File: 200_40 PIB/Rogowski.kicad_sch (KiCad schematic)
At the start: 8 parts, among them J6 53261-0271, U11 OP37

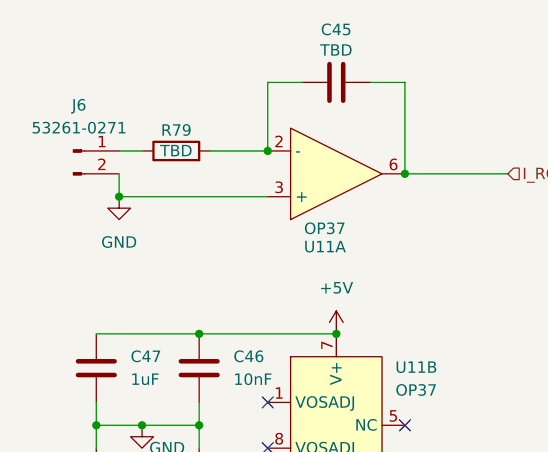
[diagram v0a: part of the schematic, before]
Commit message: assign PIB footprints, push ioc file to CubeMX 6.18.1
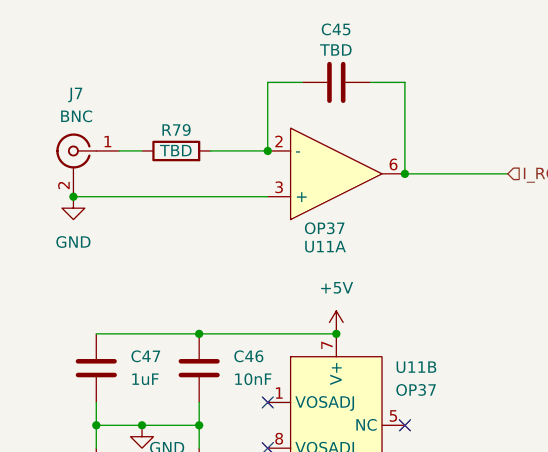
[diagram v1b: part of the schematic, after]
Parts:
- removed J6: 53261-0271, Connector_Molex:Molex_PicoBlade_53261-0271_1x02-1MP_P1.25mm_Horizontal, symbol Connector:Conn_01x02_Pin
- added J7: BNC, Connector_Coaxial:BNC_Amphenol_B6252HB-NPP3G-50_Horizontal, symbol Connector:Conn_Coaxial
- C45, C46, C47, C48, C49: footprint (none) -> Capacitor_SMD:C_0603_1608Metric
- R79: footprint (none) -> Resistor_SMD:R_0603_1608Metric
- U11: footprint Package_TO_SOT_SMD:SOT-353_SC-70-5 -> Package_SO:SOIC-8_3.9x4.9mm_P1.27mm
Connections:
- net GND: now also J7.2 (Ext)
- net at R79.1: now also J7.1 (In)
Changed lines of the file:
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@@
+	)
+	(junction
+		(at 54.61 71.12)
+		(diameter 0)
+		(color 0 0 0 0)
 	)
 	(junction
@@
 	)
 	(junction
-		(at 59.69 71.12)
-		(diameter 0)
-		(color 0 0 0 0)
-	)
-	(junction
 		(at 68.58 96.52)
 		(diameter 0)
@@
 	(wire
 		(pts
-			(xy 59.69 71.12) (xy 76.2 71.12)
+			(xy 54.61 71.12) (xy 76.2 71.12)
 		)
 		(stroke
@@
 		(pts
 			(xy 91.44 68.58) (xy 91.44 58.42)
-		)
-		(stroke
-			(width 0)
-			(type default)
-		)
-	)
-	(wire
-		(pts
-			(xy 59.69 71.12) (xy 59.69 68.58)
 		)
 		(stroke
@@
 			)
 		)
-		(property "Footprint" "Package_TO_SOT_SMD:SOT-353_SC-70-5"
+		(property "Footprint" "Package_SO:SOIC-8_3.9x4.9mm_P1.27mm"
 			(at 82.55 73.66 0)
 			(hide yes)
@@
 			)
 		)
-		(property "Footprint" ""
+		(property "Footprint" "Capacitor_SMD:C_0603_1608Metric"
 			(at 58.1152 93.98 0)
 			(hide yes)
@@
 				(path "/2bb2e4a1-de70-477a-a246-143db0a21e08/177725a5-a22e-4ba6-aa4d-305743e89374"
 					(reference "C47")
-					(unit 1)
-				)
-			)
-		)
-	)
-	(symbol
-		(lib_id "Connector:Conn_01x02_Pin")
-		(at 54.61 66.04 0)
-		(unit 1)
-		(body_style 1)
-		(exclude_from_sim no)
-		(in_bom yes)
-		(on_board yes)
-		(in_pos_files yes)
-		(dnp no)
-		(fields_autoplaced yes)
-		(property "Reference" "J6"
-			(at 55.245 60.96 0)
-			(show_name no)
-			(do_not_autoplace no)
-			(effects
-				(font
-					(size 1.27 1.27)
-				)
-			)
-		)
-		(property "Value" "53261-0271"
-			(at 55.245 63.5 0)
-			(show_name no)
-			(do_not_autoplace no)
-			(effects
-				(font
-					(size 1.27 1.27)
-				)
-			)
-		)
-		(property "Footprint" "Connector_Molex:Molex_PicoBlade_53261-0271_1x02-1MP_P1.25mm_Horizontal"
-			(at 54.61 66.04 0)
-			(hide yes)
-			(show_name no)
-			(do_not_autoplace no)
-			(effects
-				(font
-					(size 1.27 1.27)
-				)
-			)
-		)
-		(property "Datasheet" ""
-			(at 54.61 66.04 0)
-			(hide yes)
-			(show_name no)
-			(do_not_autoplace no)
-			(effects
-				(font
-					(size 1.27 1.27)
-				)
-			)
-		)
-		(property "Description" "Generic connector, single row, 01x02, script generated"
-			(at 54.61 66.04 0)
-			(hide yes)
-			(show_name no)
-			(do_not_autoplace no)
-			(effects
-				(font
-					(size 1.27 1.27)
-				)
-			)
-		)
-		(pin "2"
-		)
-		(pin "1"
-		)
-		(instances
-			(project "PIB"
-				(path "/2bb2e4a1-de70-477a-a246-143db0a21e08/177725a5-a22e-4ba6-aa4d-305743e89374"
-					(reference "J6")
 					(unit 1)
 				)
@@
 			)
 		)
-		(property "Footprint" ""
+		(property "Footprint" "Capacitor_SMD:C_0603_1608Metric"
 			(at 69.5452 106.68 0)
 			(hide yes)
@@
 				(path "/2bb2e4a1-de70-477a-a246-143db0a21e08/177725a5-a22e-4ba6-aa4d-305743e89374"
 					(reference "C49")
+					(unit 1)
+				)
+			)
+		)
+	)
+	(symbol
+		(lib_id "Connector:Conn_Coaxial")
+		(at 54.61 66.04 0)
+		(mirror y)
+		(unit 1)
+		(body_style 1)
+		(exclude_from_sim no)
+		(in_bom yes)
+		(on_board yes)
+		(in_pos_files yes)
+		(dnp no)
+		(fields_autoplaced yes)
+		(property "Reference" "J7"
+			(at 54.9274 59.69 0)
+			(show_name no)
+			(do_not_autoplace no)
+			(effects
+				(font
+					(size 1.27 1.27)
+				)
+			)
+		)
+		(property "Value" "BNC"
+			(at 54.9274 62.23 0)
+			(show_name no)
+			(do_not_autoplace no)
+			(effects
+				(font
+					(size 1.27 1.27)
+				)
+			)
+		)
+		(property "Footprint" "Connector_Coaxial:BNC_Amphenol_B6252HB-NPP3G-50_Horizontal"
+			(at 54.61 66.04 0)
+			(hide yes)
+			(show_name no)
+			(do_not_autoplace no)
+			(effects
+				(font
+					(size 1.27 1.27)
+				)
+			)
+		)
+		(property "Datasheet" ""
+			(at 54.61 66.04 0)
+			(hide yes)
+			(show_name no)
+			(do_not_autoplace no)
+			(effects
+				(font
+					(size 1.27 1.27)
+				)
+			)
+		)
+		(property "Description" "coaxial connector (BNC, SMA, SMB, SMC, Cinch/RCA, LEMO, ...)"
+			(at 54.61 66.04 0)
+			(hide yes)
+			(show_name no)
+			(do_not_autoplace no)
+			(effects
+				(font
+					(size 1.27 1.27)
+				)
+			)
+		)
+		(pin "1"
+		)
+		(pin "2"
+		)
+		(instances
+			(project "PIB"
+				(path "/2bb2e4a1-de70-477a-a246-143db0a21e08/177725a5-a22e-4ba6-aa4d-305743e89374"
+					(reference "J7")
 					(unit 1)
 				)
@@
 			)
 		)
-		(property "Footprint" ""
+		(property "Footprint" "Capacitor_SMD:C_0603_1608Metric"
 			(at 69.5452 93.98 0)
 			(hide yes)
@@
 			)
 		)
-		(property "Footprint" ""
+		(property "Footprint" "Capacitor_SMD:C_0603_1608Metric"
 			(at 58.1152 106.68 0)
 			(hide yes)
@@
 			)
 		)
-		(property "Footprint" ""
+		(property "Footprint" "Capacitor_SMD:C_0603_1608Metric"
 			(at 87.63 57.4548 0)
 			(hide yes)
@@
 			)
 		)
-		(property "Footprint" "Package_TO_SOT_SMD:SOT-353_SC-70-5"
+		(property "Footprint" "Package_SO:SOIC-8_3.9x4.9mm_P1.27mm"
 			(at 83.82 86.36 0)
 			(hide yes)
@@
 			)
 		)
-		(property "Footprint" ""
+		(property "Footprint" "Resistor_SMD:R_0603_1608Metric"
 			(at 66.04 67.818 90)
 			(hide yes)
@@
 	(symbol
 		(lib_id "power:GND")
-		(at 59.69 71.12 0)
+		(at 54.61 71.12 0)
 		(unit 1)
 		(body_style 1)
@@
 		(fields_autoplaced yes)
 		(property "Reference" "#PWR073"
-			(at 59.69 77.47 0)
+			(at 54.61 77.47 0)
 			(hide yes)
 			(show_name no)
@@
 		)
 		(property "Value" "GND"
-			(at 59.69 76.2 0)
+			(at 54.61 76.2 0)
 			(show_name no)
 			(do_not_autoplace no)
@@
 		)
 		(property "Footprint" ""
-			(at 59.69 71.12 0)
+			(at 54.61 71.12 0)
 			(hide yes)
 			(show_name no)
@@
 		)
 		(property "Datasheet" ""
-			(at 59.69 71.12 0)
+			(at 54.61 71.12 0)
 			(hide yes)
 			(show_name no)
@@
 		)
 		(property "Description" "Power symbol creates a global label with name \"GND\" , ground"
-			(at 59.69 71.12 0)
-			(hide yes)
-			(show_name no)
+			(at 54.61 71.12 0)
+			(hide yes)
+			(show_name no)

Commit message: prelim layout for pib mainboard v1. TODO review
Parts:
- C46, C49: footprint Capacitor_SMD:C_0603_1608Metric -> Capacitor_SMD:C_0402_1005Metric
- J7: value BNC -> MMCX; footprint Connector_Coaxial:BNC_Amphenol_B6252HB-NPP3G-50_Horizontal -> Connector_Coaxial:MMCX_Molex_73415-1471_Vertical
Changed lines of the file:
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@@
+	)
+	(junction
+		(at 54.61 71.12)
+		(diameter 0)
+		(color 0 0 0 0)
 	)
 	(junction
 		(at 83.82 106.68)
-		(diameter 0)
-		(color 0 0 0 0)
-	)
-	(junction
-		(at 54.61 71.12)
 		(diameter 0)
 		(color 0 0 0 0)
@@
 			)
 		)
-		(property "Footprint" "Capacitor_SMD:C_0603_1608Metric"
+		(property "Footprint" "Capacitor_SMD:C_0402_1005Metric"
 			(at 69.5452 106.68 0)
 			(hide yes)
@@
 				(path "/2bb2e4a1-de70-477a-a246-143db0a21e08/177725a5-a22e-4ba6-aa4d-305743e89374"
 					(reference "C49")
+					(unit 1)
+				)
+			)
+		)
+	)
+	(symbol
+		(lib_id "Device:C")
+		(at 68.58 90.17 0)
+		(unit 1)
+		(body_style 1)
+		(exclude_from_sim no)
+		(in_bom yes)
+		(on_board yes)
+		(in_pos_files yes)
+		(dnp no)
+		(fields_autoplaced yes)
+		(property "Reference" "C46"
+			(at 72.39 88.8999 0)
+			(show_name no)
+			(do_not_autoplace no)
+			(effects
+				(font
+					(size 1.27 1.27)
+				)
+				(justify left)
+			)
+		)
+		(property "Value" "10nF"
+			(at 72.39 91.4399 0)
+			(show_name no)
+			(do_not_autoplace no)
+			(effects
+				(font
+					(size 1.27 1.27)
+				)
+				(justify left)
+			)
+		)
+		(property "Footprint" "Capacitor_SMD:C_0402_1005Metric"
+			(at 69.5452 93.98 0)
+			(hide yes)
+			(show_name no)
+			(do_not_autoplace no)
+			(effects
+				(font
+					(size 1.27 1.27)
+				)
+			)
+		)
+		(property "Datasheet" ""
+			(at 68.58 90.17 0)
+			(hide yes)
+			(show_name no)
+			(do_not_autoplace no)
+			(effects
+				(font
+					(size 1.27 1.27)
+				)
+			)
+		)
+		(property "Description" "Unpolarized capacitor"
+			(at 68.58 90.17 0)
+			(hide yes)
+			(show_name no)
+			(do_not_autoplace no)
+			(effects
+				(font
+					(size 1.27 1.27)
+				)
+			)
+		)
+		(pin "2"
+		)
+		(pin "1"
+		)
+		(instances
+			(project "PIB"
+				(path "/2bb2e4a1-de70-477a-a246-143db0a21e08/177725a5-a22e-4ba6-aa4d-305743e89374"
+					(reference "C46")
+					(unit 1)
+				)
+			)
+		)
+	)
+	(symbol
+		(lib_id "power:+5V")
+		(at 83.82 86.36 0)
+		(unit 1)
+		(body_style 1)
+		(exclude_from_sim no)
+		(in_bom yes)
+		(on_board yes)
+		(in_pos_files yes)
+		(dnp no)
+		(fields_autoplaced yes)
+		(property "Reference" "#PWR061"
+			(at 83.82 90.17 0)
+			(hide yes)
+			(show_name no)
+			(do_not_autoplace no)
+			(effects
+				(font
+					(size 1.27 1.27)
+				)
+			)
+		)
+		(property "Value" "+5V"
+			(at 83.82 81.28 0)
+			(show_name no)
+			(do_not_autoplace no)
+			(effects
+				(font
+					(size 1.27 1.27)
+				)
+			)
+		)
+		(property "Footprint" ""
+			(at 83.82 86.36 0)
+			(hide yes)
+			(show_name no)
+			(do_not_autoplace no)
+			(effects
+				(font
+					(size 1.27 1.27)
+				)
+			)
+		)
+		(property "Datasheet" ""
+			(at 83.82 86.36 0)
+			(hide yes)
+			(show_name no)
+			(do_not_autoplace no)
+			(effects
+				(font
+					(size 1.27 1.27)
+				)
+			)
+		)
+		(property "Description" "Power symbol creates a global label with name \"+5V\""
+			(at 83.82 86.36 0)
+			(hide yes)
+			(show_name no)
+			(do_not_autoplace no)
+			(effects
+				(font
+					(size 1.27 1.27)
+				)
+			)
+		)
+		(pin "1"
+		)
+		(instances
+			(project "PIB"
+				(path "/2bb2e4a1-de70-477a-a246-143db0a21e08/177725a5-a22e-4ba6-aa4d-305743e89374"
+					(reference "#PWR061")
 					(unit 1)
 				)
@@
 			)
 		)
-		(property "Value" "BNC"
+		(property "Value" "MMCX"
 			(at 54.9274 62.23 0)
 			(show_name no)
@@
 			)
 		)
-		(property "Footprint" "Connector_Coaxial:BNC_Amphenol_B6252HB-NPP3G-50_Horizontal"
+		(property "Footprint" "Connector_Coaxial:MMCX_Molex_73415-1471_Vertical"
 			(at 54.61 66.04 0)
 			(hide yes)
@@
 			)
 		)
+		(pin "2"
+		)
 		(pin "1"
-		)
-		(pin "2"
 		)
 		(instances
@@
 					(unit 1)
 				)
-			)
-		)
-	)
-	(symbol
-		(lib_id "Device:C")
-		(at 68.58 90.17 0)
-		(unit 1)
-		(body_style 1)
-		(exclude_from_sim no)
-		(in_bom yes)
-		(on_board yes)
-		(in_pos_files yes)
-		(dnp no)
-		(fields_autoplaced yes)
-		(property "Reference" "C46"
-			(at 72.39 88.8999 0)
-			(show_name no)
-			(do_not_autoplace no)
-			(effects
-				(font
-					(size 1.27 1.27)
-				)
-				(justify left)
-			)
-		)
-		(property "Value" "10nF"
-			(at 72.39 91.4399 0)
-			(show_name no)
-			(do_not_autoplace no)
-			(effects
-				(font
-					(size 1.27 1.27)
-				)
-				(justify left)
-			)
-		)
-		(property "Footprint" "Capacitor_SMD:C_0603_1608Metric"
-			(at 69.5452 93.98 0)
-			(hide yes)
-			(show_name no)
-			(do_not_autoplace no)
-			(effects
-				(font
-					(size 1.27 1.27)
-				)
-			)
-		)
-		(property "Datasheet" ""
-			(at 68.58 90.17 0)
-			(hide yes)
-			(show_name no)
-			(do_not_autoplace no)
-			(effects
-				(font
-					(size 1.27 1.27)
-				)
-			)
-		)
-		(property "Description" "Unpolarized capacitor"
-			(at 68.58 90.17 0)
-			(hide yes)
-			(show_name no)
-			(do_not_autoplace no)
-			(effects
-				(font
-					(size 1.27 1.27)
-				)
-			)
-		)
-		(pin "2"
-		)
-		(pin "1"
-		)
-		(instances
-			(project "PIB"
-				(path "/2bb2e4a1-de70-477a-a246-143db0a21e08/177725a5-a22e-4ba6-aa4d-305743e89374"
-					(reference "C46")
-					(unit 1)
-				)
-			)
-		)
-	)
-	(symbol
-		(lib_id "power:+5V")
-		(at 83.82 86.36 0)
-		(unit 1)
-		(body_style 1)
-		(exclude_from_sim no)
-		(in_bom yes)
-		(on_board yes)
-		(in_pos_files yes)
-		(dnp no)
-		(fields_autoplaced yes)
-		(property "Reference" "#PWR061"
-			(at 83.82 90.17 0)
-			(hide yes)
-			(show_name no)
-			(do_not_autoplace no)
-			(effects
-				(font
-					(size 1.27 1.27)
-				)
-			)
-		)
-		(property "Value" "+5V"
-			(at 83.82 81.28 0)
-			(show_name no)
-			(do_not_autoplace no)
-			(effects
-				(font
-					(size 1.27 1.27)
-				)
-			)
-		)
-		(property "Footprint" ""
-			(at 83.82 86.36 0)
-			(hide yes)
-			(show_name no)
-			(do_not_autoplace no)
-			(effects
-				(font
-					(size 1.27 1.27)
-				)
-			)
-		)
-		(property "Datasheet" ""
-			(at 83.82 86.36 0)
-			(hide yes)
-			(show_name no)
-			(do_not_autoplace no)
-			(effects
-				(font
-					(size 1.27 1.27)
-				)
-			)
-		)
-		(property "Description" "Power symbol creates a global label with name \"+5V\""
-			(at 83.82 86.36 0)
-			(hide yes)
-			(show_name no)
-			(do_not_autoplace no)
-			(effects
-				(font
-					(size 1.27 1.27)
-				)
-			)
-		)
-		(pin "1"
-		)
-		(instances
-			(project "PIB"
-				(path "/2bb2e4a1-de70-477a-a246-143db0a21e08/177725a5-a22e-4ba6-aa4d-305743e89374"
-					(reference "#PWR061")
-					(unit 1)
-				)

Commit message: clear out claude flagged items
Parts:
- removed U11: OP37, Package_SO:SOIC-8_3.9x4.9mm_P1.27mm, symbol 0_PAY_Symbol_Library:OP37
- added C69, C70: 1uF, Capacitor_SMD:C_0603_1608Metric, symbol Device:C
- added C71, C72: 470pF, Capacitor_SMD:C_0402_1005Metric, symbol Device:C
- added D39, D40, D43, D44: BAT54J, Diode_SMD:D_SOD-323F, symbol Diode:BAT54J
- added J6: MMCX, Connector_Coaxial:MMCX_Molex_73415-1471_Vertical, symbol Connector:Conn_Coaxial
- added Q3, Q4, Q5: BSS138, Package_TO_SOT_SMD:SOT-23, symbol Transistor_FET:BSS138
- added R100, R102, R106: 100R, Resistor_SMD:R_0402_1005Metric, symbol Device:R
- added R101, R96, R97, R99: 10K, Resistor_SMD:R_0402_1005Metric, symbol Device:R
- added R104, R105: 1K, Resistor_SMD:R_0402_1005Metric, symbol Device:R
- added R95, R98: TBD, Resistor_SMD:R_0603_1608Metric, symbol Device:R
- added U11: OP27, Package_SO:SOIC-8_3.9x4.9mm_P1.27mm, symbol 0_PAY_Symbol_Library:OP27
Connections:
- net +5V: now also R99.1, U11.7 (V+)
- net -5V: now also U11.4 (V-)
- net GND: now also C70.2, C71.2, C72.2, D39.2 (A), D44.2 (A), J6.2 (Ext), Q5.2 (S), R101.2, R95.1, R97.2
- net I_ROGOWSKI: now also C71.1, R104.1; no longer C45.2
- net at C45.1, R79.2: now also Q4.2 (S), R98.1, U11.2 (-)
- net at J7.1 (In): now also C69.1, R95.2; no longer R79.1
- new net: C70.1, R96.2, R97.1, U11.3 (+)
- new net: C45.2, Q3.2 (S), R102.2, R98.2, U11.6
- new net: Q5.1 (G), R100.1, R101.1
- new net: D39.1 (K), D40.2 (A), R102.1, R104.2
- new net: D43.2 (A), D44.1 (K), R105.2, R106.1
- new net: C69.2, R79.1
- new net: Q3.1 (G), Q4.1 (G), Q5.3 (D), R99.2
- new net: Q3.3 (D), Q4.3 (D)
- new net +3.3V: D40.1 (K), D43.1 (K)
- new net ROGOWSKI_RST: R100.2
- new net VDDA: R96.1
- new net V_DCHG_IN: J6.1 (In), R106.2
- new net V_DISCHARGE: C72.1, R105.1
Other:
- moved on the sheet: C46, C47, C48, C49, J7

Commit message: clod
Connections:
- net ROGOWSKI_RST renamed ~{ROGOWSKI_RST}
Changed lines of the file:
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@@
 	)
 	(hierarchical_label "V_DISCHARGE"
-		(shape input)
+		(shape output)
 		(at 110.49 152.4 0)
 		(effects
@@
 		)
 	)
-	(hierarchical_label "ROGOWSKI_RST"
+	(hierarchical_label "~{ROGOWSKI_RST}"
 		(shape input)
 		(at 48.26 40.64 180)
@@
 	)
 	(hierarchical_label "I_ROGOWSKI"
-		(shape input)
+		(shape output)
 		(at 129.54 68.58 0)
 		(effects

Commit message: lots of claude close outs
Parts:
- added D38: SD12C-01F, Diode_SMD:D_SOD-323, symbol Diode:SD12C-01F
- C45: value TBD -> 10nF C0G
- C69: value 1uF -> 4.7uF
- R79: value TBD -> 2K
- R95: value TBD -> 100K
- R98: value TBD -> 1M
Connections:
- net GND: now also D38.1 (A1)
- net at C69.1, J7.1 (In), R95.2: now also D38.2 (A2)
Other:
- moved on the sheet: C45, C46, C47, C48, C49, C69, C70, C71, C72, D39, D40, D43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

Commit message: select lower leakage part for integrator reset
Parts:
- removed Q3, Q4, Q5: BSS138, Package_TO_SOT_SMD:SOT-23, symbol Transistor_FET:BSS138
- added Q3, Q4, Q5: BSS131, Package_TO_SOT_SMD:SOT-23, symbol 0_PAY_Symbol_Library:BSS131
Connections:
- net GND: now also Q5.2 (S)
- net at C45.1, R79.2, R98.1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: now also Q4.2 (S)
- net at C45.2, R102.2, R98.2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: now also Q3.2 (S)
- net at R100.1, R101.1: now also Q5.1 (G)
- net at R99.2: now also Q3.1 (G), Q4.1 (G), Q5.3 (D)
- new net: Q3.3 (D), Q4.3 (D)

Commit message: finish routing with all critical schematic fixes
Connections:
- net VDDA is gone; now on net +3.3V: R96.1
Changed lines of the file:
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@@
 	)
 	(symbol
-		(lib_id "power:+3.3V")
-		(at 58.42 72.39 0)
-		(unit 1)
-		(body_style 1)
-		(exclude_from_sim no)
-		(in_bom yes)
-		(on_board yes)
-		(in_pos_files yes)
-		(dnp no)
-		(property "Reference" "#PWR0155"
-			(at 58.42 76.2 0)
-			(hide yes)
-			(show_name no)
-			(do_not_autoplace no)
-			(effects
-				(font
-					(size 1.27 1.27)
-				)
-			)
-		)
-		(property "Value" "VDDA"
-			(at 58.42 67.818 0)
-			(show_name no)
-			(do_not_autoplace no)
-			(effects
-				(font
-					(size 1.27 1.27)
-				)
-			)
-		)
-		(property "Footprint" ""
-			(at 58.42 72.39 0)
-			(hide yes)
-			(show_name no)
-			(do_not_autoplace no)
-			(effects
-				(font
-					(size 1.27 1.27)
-				)
-			)
-		)
-		(property "Datasheet" ""
-			(at 58.42 72.39 0)
-			(hide yes)
-			(show_name no)
-			(do_not_autoplace no)
-			(effects
-				(font
-					(size 1.27 1.27)
-				)
-			)
-		)
-		(property "Description" "Power symbol creates a global label with name \"+3.3V\""
-			(at 58.42 72.39 0)
-			(hide yes)
-			(show_name no)
-			(do_not_autoplace no)
-			(effects
-				(font
-					(size 1.27 1.27)
-				)
-			)
-		)
-		(pin "1"
-		)
-		(instances
-			(project "PIB"
-				(path "/2bb2e4a1-de70-477a-a246-143db0a21e08/177725a5-a22e-4ba6-aa4d-305743e89374"
-					(reference "#PWR0155")
-					(unit 1)
-				)
-			)
-		)
-	)
-	(symbol
 		(lib_id "power:GND")
 		(at 77.47 119.38 0)
@@
 					(unit 1)
 				)
+			)
+		)
+	)
+	(symbol
+		(lib_id "power:+3.3V")
+		(at 58.42 72.39 0)
+		(unit 1)
+		(body_style 1)
+		(exclude_from_sim no)
+		(in_bom yes)
+		(on_board yes)
+		(in_pos_files yes)
+		(dnp no)
+		(property "Reference" "#PWR0155"
+			(at 58.42 76.2 0)
+			(hide yes)
+			(show_name no)
+			(do_not_autoplace no)
+			(effects
+				(font
+					(size 1.27 1.27)
+				)
+			)
+		)
+		(property "Value" "+3.3V"
+			(at 58.42 67.818 0)
+			(show_name no)
+			(do_not_autoplace no)
+			(effects
+				(font
+					(size 1.27 1.27)
+				)
+			)
+		)
+		(property "Footprint" ""
+			(at 58.42 72.39 0)
+			(hide yes)
+			(show_name no)
+			(do_not_autoplace no)
+			(effects
+				(font
+					(size 1.27 1.27)
+				)
+			)
+		)
+		(property "Datasheet" ""
+			(at 58.42 72.39 0)
+			(hide yes)
+			(show_name no)
+			(do_not_autoplace no)
+			(effects
+				(font
+					(size 1.27 1.27)
+				)
+			)
+		)
+		(property "Description" "Power symbol creates a global label with name \"+3.3V\""
+			(at 58.42 72.39 0)
+			(hide yes)
+			(show_name no)
+			(do_not_autoplace no)
+			(effects
+				(font
+					(size 1.27 1.27)
+				)
+			)
+		)
+		(pin "1"
+		)
+		(instances
+			(project "PIB"
+				(path "/2bb2e4a1-de70-477a-a246-143db0a21e08/177725a5-a22e-4ba6-aa4d-305743e89374"
+					(reference "#PWR0155")
+					(unit 1)
+				)

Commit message: Assign MPNs and digikey PNs, export gerbers & bom. PIB Mainboard Rev 1.0 Release
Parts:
- C45: Digikey PN (none) -> 490-GRT1885C1E103FA02DCT-ND; MP (none) -> GRT1885C1E103FA02D
- C46, C49: Digikey PN (none) -> 490-4516-1-ND; MP (none) -> GRM155R71H103KA88D
- C47, C48, C70: Digikey PN (none) -> 587-3352-1-ND; MP (none) -> GMK107AB7105KAHT
- C69: Digikey PN (none) -> 4713-GMC10X7R475K16NTCT-ND; MP (none) -> GMC10X7R475K16NT
- C71, C72: Digikey PN (none) -> 490-GCM1555C1H471FA16DCT-ND; MP (none) -> GCM1555C1H471FA16D
- D38: value SD12C-01F -> SD12C.TCT; Digikey PN (none) -> SD12C.TCTCT-ND; MP (none) -> SD12C.TCT
- D39, D40, D43, D44: value BAT54J -> BAT54WS; Digikey PN (none) -> 4878-BAT54WSCT-ND; MP (none) -> BAT54WS
- J6, J7: Digikey PN (none) -> WM5557-ND; MP (none) -> 73415-1471
- Q3, Q4, Q5: value BSS131 -> BSS123N; Digikey PN (none) -> BSS123NH6327XTSA1CT-ND; MP (none) -> BSS123NH6327XTSA1
- R100, R102, R106: Digikey PN (none) -> YAG2301CT-ND; MP (none) -> RT0402BRD07100RL
- R101, R96, R97, R99: Digikey PN (none) -> YAG1346CT-ND; MP (none) -> RT0402BRD0710KL
- R104, R105: Digikey PN (none) -> 13-RT0402BRD131KLCT-ND; MP (none) -> RT0402BRD131KL
- R79: Digikey PN (none) -> P2.0KDBCT-ND; MP (none) -> ERA-3AEB202V
- R95: Digikey PN (none) -> 2019-RN73R1JTTD1003B25CT-ND; MP (none) -> RN73R1JTTD1003B25
- R98: Digikey PN (none) -> 2019-RN73H1JTTD1004B25CT-ND; MP (none) -> RN73H1JTTD1004B25
- U11: Digikey PN (none) -> 505-OP27GSZ-ND; MP (none) -> OP27GSZ
